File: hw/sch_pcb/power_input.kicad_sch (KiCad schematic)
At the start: 23 parts

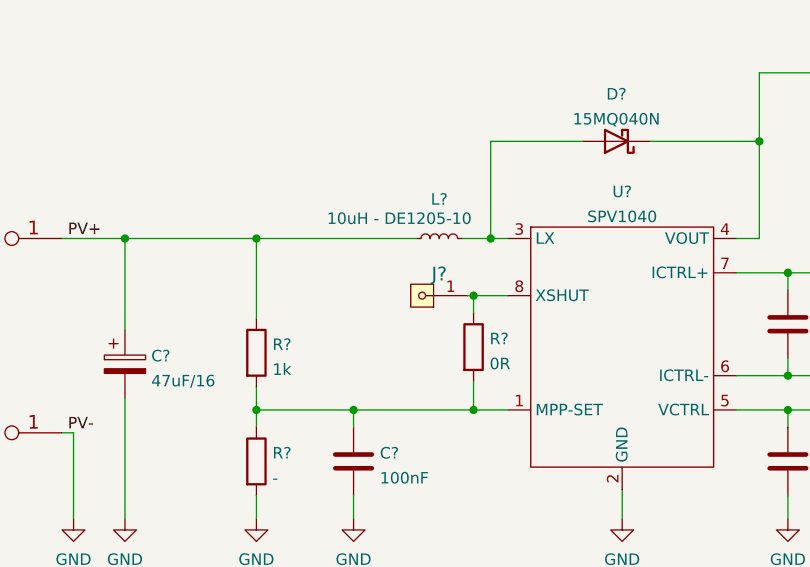
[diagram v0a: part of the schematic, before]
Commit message: cleanup unused file.
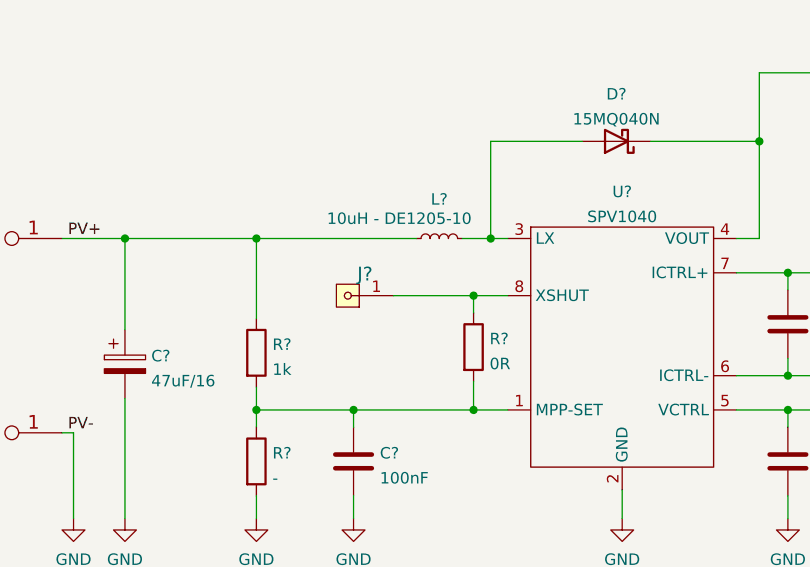
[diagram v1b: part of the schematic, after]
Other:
- moved on the sheet: J?
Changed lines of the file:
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@@
     (stroke (width 0) (type default) (color 0 0 0 0))
   )
-  (wire (pts (xy 106.68 88.265) (xy 106.045 88.265))
+  (wire (pts (xy 97.79 88.265) (xy 106.68 88.265))
     (stroke (width 0) (type default) (color 0 0 0 0))
   )
@@
     (pin "2")
   )
-  (symbol (lib_id "MLAB_HEADER:HEADER_1x01") (at 100.965 88.265 180) (unit 1)
-    (in_bom yes) (on_board yes) (fields_autoplaced)
-    (property "Reference" "J?" (id 0) (at 102.87 85.8701 0)
+  (symbol (lib_id "MLAB_HEADER:HEADER_1x01") (at 92.71 88.265 180) (unit 1)
+    (in_bom yes) (on_board yes) (fields_autoplaced)
+    (property "Reference" "J?" (id 0) (at 94.615 85.8701 0)
       (effects (font (size 1.524 1.524)))
     )
-    (property "Value" "HEADER_1x01" (id 1) (at 102.87 85.8701 0)
+    (property "Value" "HEADER_1x01" (id 1) (at 94.615 85.8701 0)
       (effects (font (size 1.524 1.524)) hide)
     )
-    (property "Footprint" "Mlab_Pin_Headers:Straight_1x01" (id 2) (at 102.87 85.8701 0)
+    (property "Footprint" "Mlab_Pin_Headers:Straight_1x01" (id 2) (at 94.615 85.8701 0)
       (effects (font (size 1.524 1.524)) hide)
     )
-    (property "Datasheet" "" (id 3) (at 100.965 88.265 0)
+    (property "Datasheet" "" (id 3) (at 92.71 88.265 0)
       (effects (font (size 1.524 1.524)))
     )

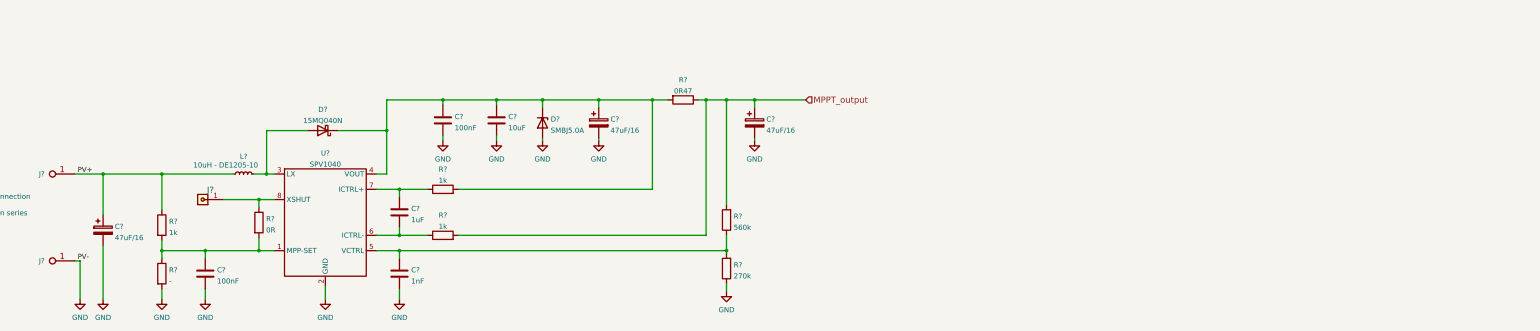
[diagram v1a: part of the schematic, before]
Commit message: finish gauge schematics design.
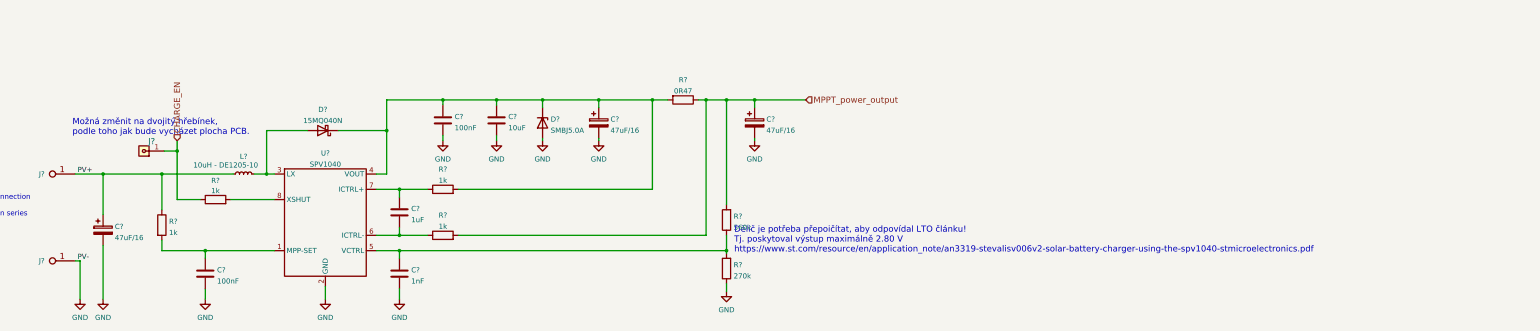
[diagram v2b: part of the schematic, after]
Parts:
- removed R?: -, Resistor_SMD:R_0805_2012Metric, symbol Device:R
- R?: value 0R -> 1k
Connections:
- net at C?.1, R?.2, U?.1 (MPP-SET): no longer R?.2
- net CHARGE_EN: now reaches J?.1, R?.1
- net CHARGE_EN: no longer U?.8 (XSHUT)
- net MPPT_output renamed MPPT_power_output
- new net: R?.2, U?.8 (XSHUT)
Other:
- note added: "Dělič je potřeba přepoičítat, aby odpovídal LTO článku! Tj. poskytoval výstup maximálně 2.80 V https://www.st.com/resource/en/application_note/an3319-stevalisv006v2-solar-battery-charger-using-the-spv1040-stmicroelectronics.pdf"
- note added: "Možná změnit na dvojitý hřebínek, podle toho jak bude vycházet plocha PCB."
- moved on the sheet: J?, R?
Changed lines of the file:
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@@
 (kicad_sch (version 20211123) (generator eeschema)
   (paper "A4")
+  (title_block
+    (date "2022-07-20")
+    (comment 2 "Solar charged LTO Battery Managment System")
+  )
   (junction (at 217.805 63.5) (diameter 0) (color 0 0 0 0)
   )
@@
   (junction (at 222.885 63.5) (diameter 0) (color 0 0 0 0)
   )
-  (junction (at 106.68 100.965) (diameter 0) (color 0 0 0 0)
-  )
-  (junction (at 106.68 88.265) (diameter 0) (color 0 0 0 0)
-  )
   (junction (at 177.165 63.5) (diameter 0) (color 0 0 0 0)
   )
@@
   (junction (at 191.135 63.5) (diameter 0) (color 0 0 0 0)
   )
-  (junction (at 82.55 100.965) (diameter 0) (color 0 0 0 0)
-  )
   (junction (at 141.605 100.965) (diameter 0) (color 0 0 0 0)
   )
+  (junction (at 86.36 76.2) (diameter 0) (color 0 0 0 0)
+  )
   (junction (at 93.345 100.965) (diameter 0) (color 0 0 0 0)
   )
@@
     (stroke (width 0) (type default) (color 0 0 0 0))
   )
-  (wire (pts (xy 82.55 113.03) (xy 82.55 110.49))
+  (wire (pts (xy 86.36 73.66) (xy 86.36 76.2))
     (stroke (width 0) (type default) (color 0 0 0 0))
   )
@@
     (stroke (width 0) (type default) (color 0 0 0 0))
   )
-  (wire (pts (xy 106.68 100.965) (xy 106.68 97.79))
-    (stroke (width 0) (type default) (color 0 0 0 0))
-  )
   (wire (pts (xy 165.735 63.5) (xy 177.165 63.5))
     (stroke (width 0) (type default) (color 0 0 0 0))
@@
     (stroke (width 0) (type default) (color 0 0 0 0))
   )
+  (wire (pts (xy 86.36 76.2) (xy 86.36 88.265))
+    (stroke (width 0) (type default) (color 0 0 0 0))
+  )
   (wire (pts (xy 156.21 85.725) (xy 204.47 85.725))
     (stroke (width 0) (type default) (color 0 0 0 0))
@@
     (stroke (width 0) (type default) (color 0 0 0 0))
   )
-  (wire (pts (xy 106.68 88.265) (xy 106.68 90.17))
-    (stroke (width 0) (type default) (color 0 0 0 0))
-  )
   (wire (pts (xy 156.21 97.155) (xy 217.805 97.155))
     (stroke (width 0) (type default) (color 0 0 0 0))
@@
     (stroke (width 0) (type default) (color 0 0 0 0))
   )
-  (wire (pts (xy 110.49 88.265) (xy 106.68 88.265))
+  (wire (pts (xy 99.695 88.265) (xy 110.49 88.265))
     (stroke (width 0) (type default) (color 0 0 0 0))
   )
@@
     (stroke (width 0) (type default) (color 0 0 0 0))
   )
+  (wire (pts (xy 83.185 76.2) (xy 86.36 76.2))
+    (stroke (width 0) (type default) (color 0 0 0 0))
+  )
   (wire (pts (xy 229.87 73.025) (xy 229.87 73.66))
     (stroke (width 0) (type default) (color 0 0 0 0))
@@
     (stroke (width 0) (type default) (color 0 0 0 0))
   )
-  (wire (pts (xy 106.68 100.965) (xy 93.345 100.965))
-    (stroke (width 0) (type default) (color 0 0 0 0))
-  )
   (wire (pts (xy 138.43 63.5) (xy 152.4 63.5))
     (stroke (width 0) (type default) (color 0 0 0 0))
@@
     (stroke (width 0) (type default) (color 0 0 0 0))
   )
+  (wire (pts (xy 86.36 88.265) (xy 92.075 88.265))
+    (stroke (width 0) (type default) (color 0 0 0 0))
+  )
   (wire (pts (xy 126.365 71.12) (xy 138.43 71.12))
     (stroke (width 0) (type default) (color 0 0 0 0))
@@
     (stroke (width 0) (type default) (color 0 0 0 0))
   )
-  (wire (pts (xy 82.55 100.965) (xy 82.55 102.87))
-    (stroke (width 0) (type default) (color 0 0 0 0))
-  )
   (wire (pts (xy 60.96 103.505) (xy 62.23 103.505))
     (stroke (width 0) (type default) (color 0 0 0 0))
   )
-  (wire (pts (xy 97.79 88.265) (xy 106.68 88.265))
-    (stroke (width 0) (type default) (color 0 0 0 0))
-  )
   (wire (pts (xy 93.345 102.87) (xy 93.345 100.965))
     (stroke (width 0) (type default) (color 0 0 0 0))
   )
-  (wire (pts (xy 110.49 100.965) (xy 106.68 100.965))
+  (wire (pts (xy 93.345 100.965) (xy 110.49 100.965))
     (stroke (width 0) (type default) (color 0 0 0 0))
   )
@@
     (effects (font (size 1.27 1.27)) (justify left bottom))
   )
+  (text "Dělič je potřeba přepoičítat, aby odpovídal LTO článku!\nTj. poskytoval výstup maximálně 2.80 V\nhttps://www.st.com/resource/en/application_note/an3319-stevalisv006v2-solar-battery-charger-using-the-spv1040-stmicroelectronics.pdf"
+    (at 224.79 101.6 0)
+    (effects (font (size 1.524 1.524)) (justify left bottom))
+  )
+  (text "Možná změnit na dvojitý hřebínek, \npodle toho jak bude vycházet plocha PCB."
+    (at 60.325 72.39 0)
+    (effects (font (size 1.524 1.524)) (justify left bottom))
+  )
   (text "Solar Cell Panel Connection" (at 111.125 29.845 0)
     (effects (font (size 2.9972 2.9972)) (justify left bottom))
@@
     (effects (font (size 1.27 1.27)) (justify left bottom))
   )
-  (hierarchical_label "MPPT_output" (shape input) (at 242.57 63.5 0)
+  (hierarchical_label "MPPT_power_output" (shape input) (at 242.57 63.5 0)
+    (effects (font (size 1.524 1.524)) (justify left))
+  )
+  (hierarchical_label "CHARGE_EN" (shape input) (at 86.36 73.66 90)
     (effects (font (size 1.524 1.524)) (justify left))
   )
@@
     )
     (pin "1")
-  )
-  (symbol (lib_id "Device:R") (at 82.55 106.68 0) (unit 1)
-    (in_bom yes) (on_board yes) (fields_autoplaced)
-    (property "Reference" "R?" (id 0) (at 84.328 105.7715 0)
-      (effects (font (size 1.27 1.27)) (justify left))
-    )
-    (property "Value" "-" (id 1) (at 84.328 108.5466 0)
-      (effects (font (size 1.27 1.27)) (justify left))
-    )
-    (property "Footprint" "Resistor_SMD:R_0805_2012Metric" (id 2) (at 80.772 106.68 90)
-      (effects (font (size 1.27 1.27)) hide)
-    )
-    (property "Datasheet" "~" (id 3) (at 82.55 106.68 0)
-      (effects (font (size 1.27 1.27)) hide)
-    )
-    (pin "1")
-    (pin "2")
   )
   (symbol (lib_id "Device:C") (at 152.4 68.58 0) (unit 1)
@@
       (effects (font (size 1.27 1.27)) hide)
     )
-    (property "Datasheet" "" (id 3) (at 123.19 88.265 0)
+    (property "Datasheet" "https://www.st.com/resource/en/datasheet/spv1040.pdf" (id 3) (at 123.19 88.265 0)
       (effects (font (size 1.27 1.27)) hide)
     )
@@
     (pin "1")
   )
-  (symbol (lib_id "power:GND") (at 82.55 113.03 0) (unit 1)
-    (in_bom yes) (on_board yes) (fields_autoplaced)
-    (property "Reference" "#PWR?" (id 0) (at 82.55 119.38 0)
-      (effects (font (size 1.27 1.27)) hide)
-    )
-    (property "Value" "GND" (id 1) (at 82.55 117.5924 0))
-    (property "Footprint" "" (id 2) (at 82.55 113.03 0)
-      (effects (font (size 1.27 1.27)) hide)
-    )
-    (property "Datasheet" "" (id 3) (at 82.55 113.03 0)
-      (effects (font (size 1.27 1.27)) hide)
-    )
-    (pin "1")
-  )
   (symbol (lib_id "Device:R") (at 82.55 94.615 0) (unit 1)
     (in_bom yes) (on_board yes) (fields_autoplaced)
@@
     (pin "2")
   )
-  (symbol (lib_id "MLAB_HEADER:HEADER_1x01") (at 92.71 88.265 180) (unit 1)
-    (in_bom yes) (on_board yes) (fields_autoplaced)
-    (property "Reference" "J?" (id 0) (at 94.615 85.8701 0)
+  (symbol (lib_id "MLAB_HEADER:HEADER_1x01") (at 78.105 76.2 180) (unit 1)
+    (in_bom yes) (on_board yes) (fields_autoplaced)
+    (property "Reference" "J?" (id 0) (at 80.01 73.8051 0)
       (effects (font (size 1.524 1.524)))
     )
-    (property "Value" "HEADER_1x01" (id 1) (at 94.615 85.8701 0)
+    (property "Value" "HEADER_1x01" (id 1) (at 80.01 73.8051 0)
       (effects (font (size 1.524 1.524)) hide)
     )
-    (property "Footprint" "Mlab_Pin_Headers:Straight_1x01" (id 2) (at 94.615 85.8701 0)
+    (property "Footprint" "Mlab_Pin_Headers:Straight_1x01" (id 2) (at 80.01 73.8051 0)
       (effects (font (size 1.524 1.524)) hide)
     )
-    (property "Datasheet" "" (id 3) (at 92.71 88.265 0)
+    (property "Datasheet" "" (id 3) (at 78.105 76.2 0)
       (effects (font (size 1.524 1.524)))
     )
@@
     (pin "1")
   )
-  (symbol (lib_id "Device:R") (at 106.68 93.98 0) (unit 1)
-    (in_bom yes) (on_board yes) (fields_autoplaced)
-    (property "Reference" "R?" (id 0) (at 108.458 93.0715 0)
-      (effects (font (size 1.27 1.27)) (justify left))
-    )
-    (property "Value" "0R" (id 1) (at 108.458 95.8466 0)
-      (effects (font (size 1.27 1.27)) (justify left))
-    )
-    (property "Footprint" "Resistor_SMD:R_0805_2012Metric" (id 2) (at 104.902 93.98 90)
-      (effects (font (size 1.27 1.27)) hide)
-    )
-    (property "Datasheet" "~" (id 3) (at 106.68 93.98 0)
-      (effects (font (size 1.27 1.27)) hide)
-    )
-    (property "UST_ID" "5c70984512875079b91f896b" (id 4) (at 106.68 93.98 0)
-      (effects (font (size 1.27 1.27)) hide)
-    )
+  (symbol (lib_id "Device:R") (at 95.885 88.265 90) (unit 1)
+    (in_bom yes) (on_board yes) (fields_autoplaced)
+    (property "Reference" "R?" (id 0) (at 95.885 83.5492 90))
+    (property "Value" "1k" (id 1) (at 95.885 86.0861 90))
+    (property "Footprint" "Resistor_SMD:R_0805_2012Metric" (id 2) (at 95.885 90.043 90)
+      (effects (font (size 1.27 1.27)) hide)
+    )
+    (property "Datasheet" "~" (id 3) (at 95.885 88.265 0)
+      (effects (font (size 1.27 1.27)) hide)
+    )
+    (property "UST_ID" "5c70984512875079b91f896b" (id 4) (at 95.885 88.265 0)
+      (effects (font (size 1.27 1.27)) hide)
+    )

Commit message: Update schematics: Adding datasheet Update title blocks Update pull-up value for CHARGE_CTRL signal.
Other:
- company: (none) -> MLAB.cz
- title: (none) -> SOLARMINIBAT01A
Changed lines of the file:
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@@
   (paper "A4")
   (title_block
+    (title "SOLARMINIBAT01A")
     (date "2022-07-20")
+    (rev "A")
+    (company "MLAB.cz")
     (comment 2 "Solar charged LTO Battery Managment System")
   )

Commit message: Edit schema
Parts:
- removed C? (x3): 47uF/16, Mlab_C:TantalC_SizeC_Reflow, symbol Device:C_Polarized
- removed J?: HEADER_1x01, Mlab_Pin_Headers:Straight_1x01, symbol MLAB_HEADER:HEADER_1x01
- added C14, C15, C8: 47uF/6V3, Capacitor_SMD:C_0805_2012Metric, symbol Device:C
- added J4: HEADER_2x01_PARALLEL, Mlab_Pin_Headers:Straight_2x01, symbol MLAB_HEADER:HEADER_2x01_PARALLEL
- C10: renamed from C?; UST_ID 5c70984712875079b91f8b50 -> (none)
- C11: renamed from C?; UST_ID 5c70984712875079b91f8b45 -> (none)
- C12, C9: renamed from C?; UST_ID 5c70984712875079b91f8b4c -> (none)
- C13: renamed from C?; UST_ID 5c70984812875079b91f8bbd -> (none)
- D10: renamed from D?; UST_ID 5c70984512875079b91f88c7 -> (none)
- D9: renamed from D?; UST_ID 5c70984512875079b91f88b0 -> (none)
- J2: renamed from J?; UST_ID 5c70984412875079b91f87c5 -> (none)
- J3: renamed from J?; UST_ID 5c70984412875079b91f87c3 -> (none)
- L1: renamed from L?; UST_ID 5c70984412875079b91f8822 -> (none)
- R17, R19, R20: renamed from R?; UST_ID 5c70984512875079b91f898c -> (none)
- R18: renamed from R?; UST_ID 5c70984512875079b91f896b -> (none)
- R21: renamed from R?; UST_ID 60be2ed51287500165e6c1cd -> (none)
- R22: renamed from R?; UST_ID 5c70984712875079b91f8aa6 -> (none)
- R23: renamed from R?; UST_ID 5c70984712875079b91f8aa0 -> (none)
- U3: renamed from U?; UST_ID 5c70984612875079b91f89bc -> (none)
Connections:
- net CHARGE_EN: now also J4.1, J4.2
- net GND: now also C14.2, C15.2, C8.2
- net MPPT_power_output: now also C15.1
- net PV+: now also C8.1
- net at C12.1, C13.1, D10.1 (K)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: now also C14.1
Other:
- note removed: "Možná změnit na dvojitý hřebínek, podle toho jak bude vycházet plocha PCB."

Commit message: Edit PCB
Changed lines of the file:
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@@
     )
     (property "Footprint" "Mlab_Pin_Headers:Straight_2x01" (id 2) (at 76.835 76.2 0)
-      (effects (font (size 1.524 1.524)))
+      (effects (font (size 1.524 1.524)) hide)
     )
     (property "Datasheet" "" (id 3) (at 76.835 76.2 0)
